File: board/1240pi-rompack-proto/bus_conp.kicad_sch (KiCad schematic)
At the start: 14 parts, among them J20 CardEdge_ROMPACK

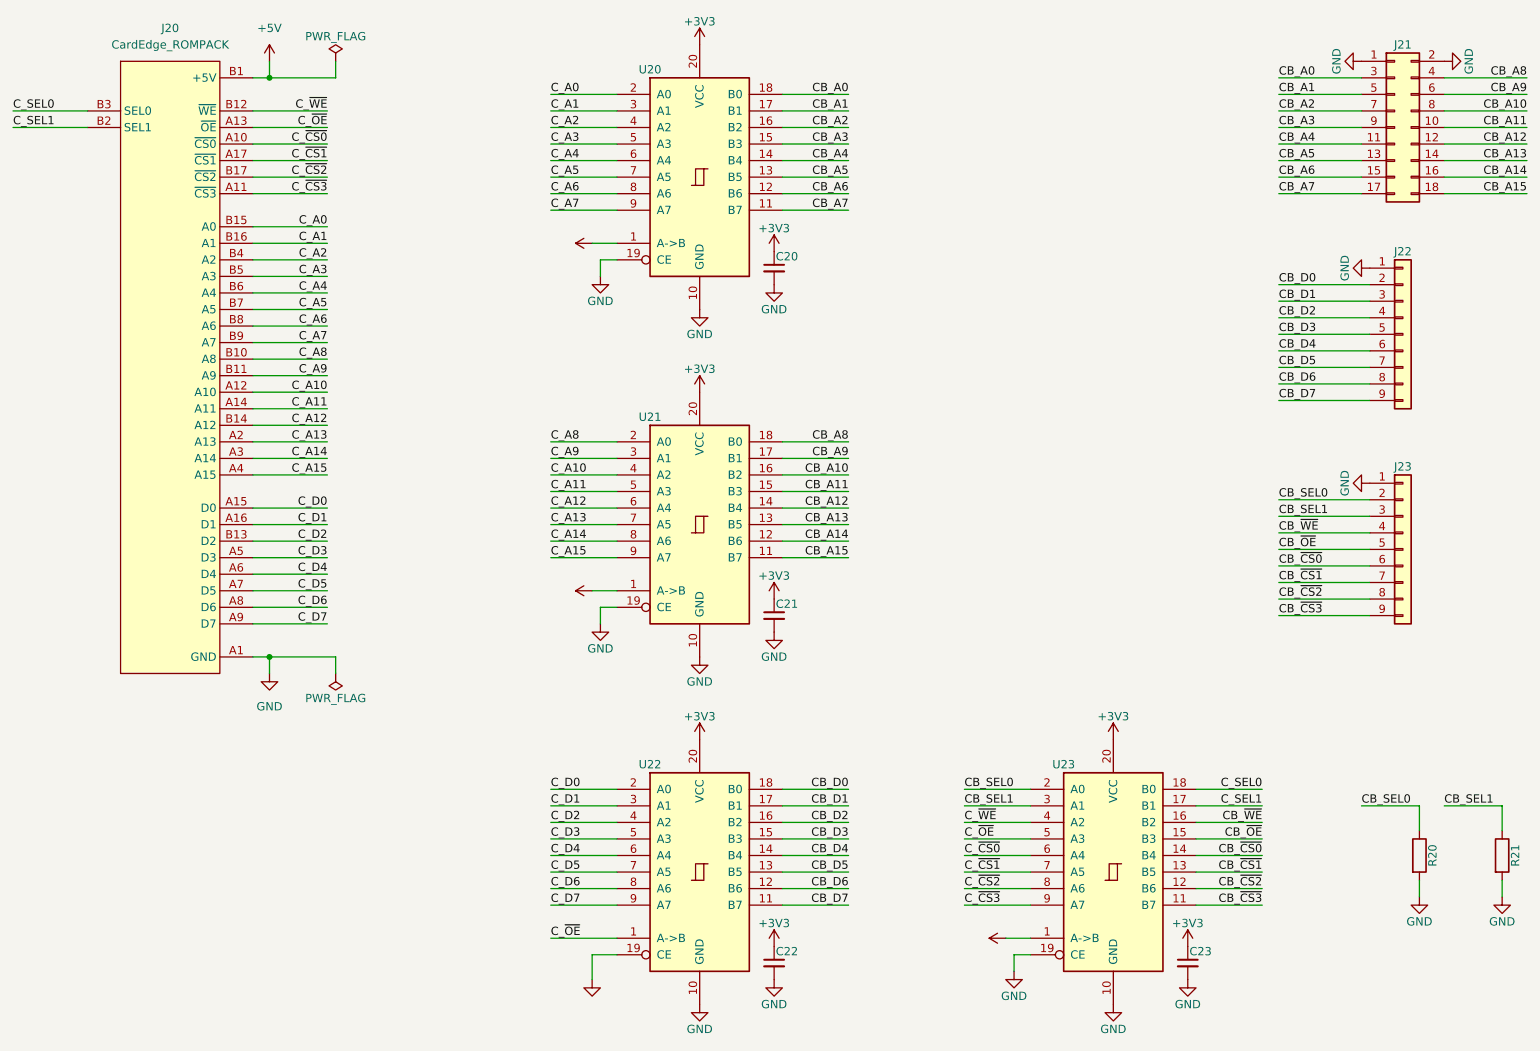
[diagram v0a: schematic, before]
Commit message: Fix names of BUSRQ and IORQ nets.
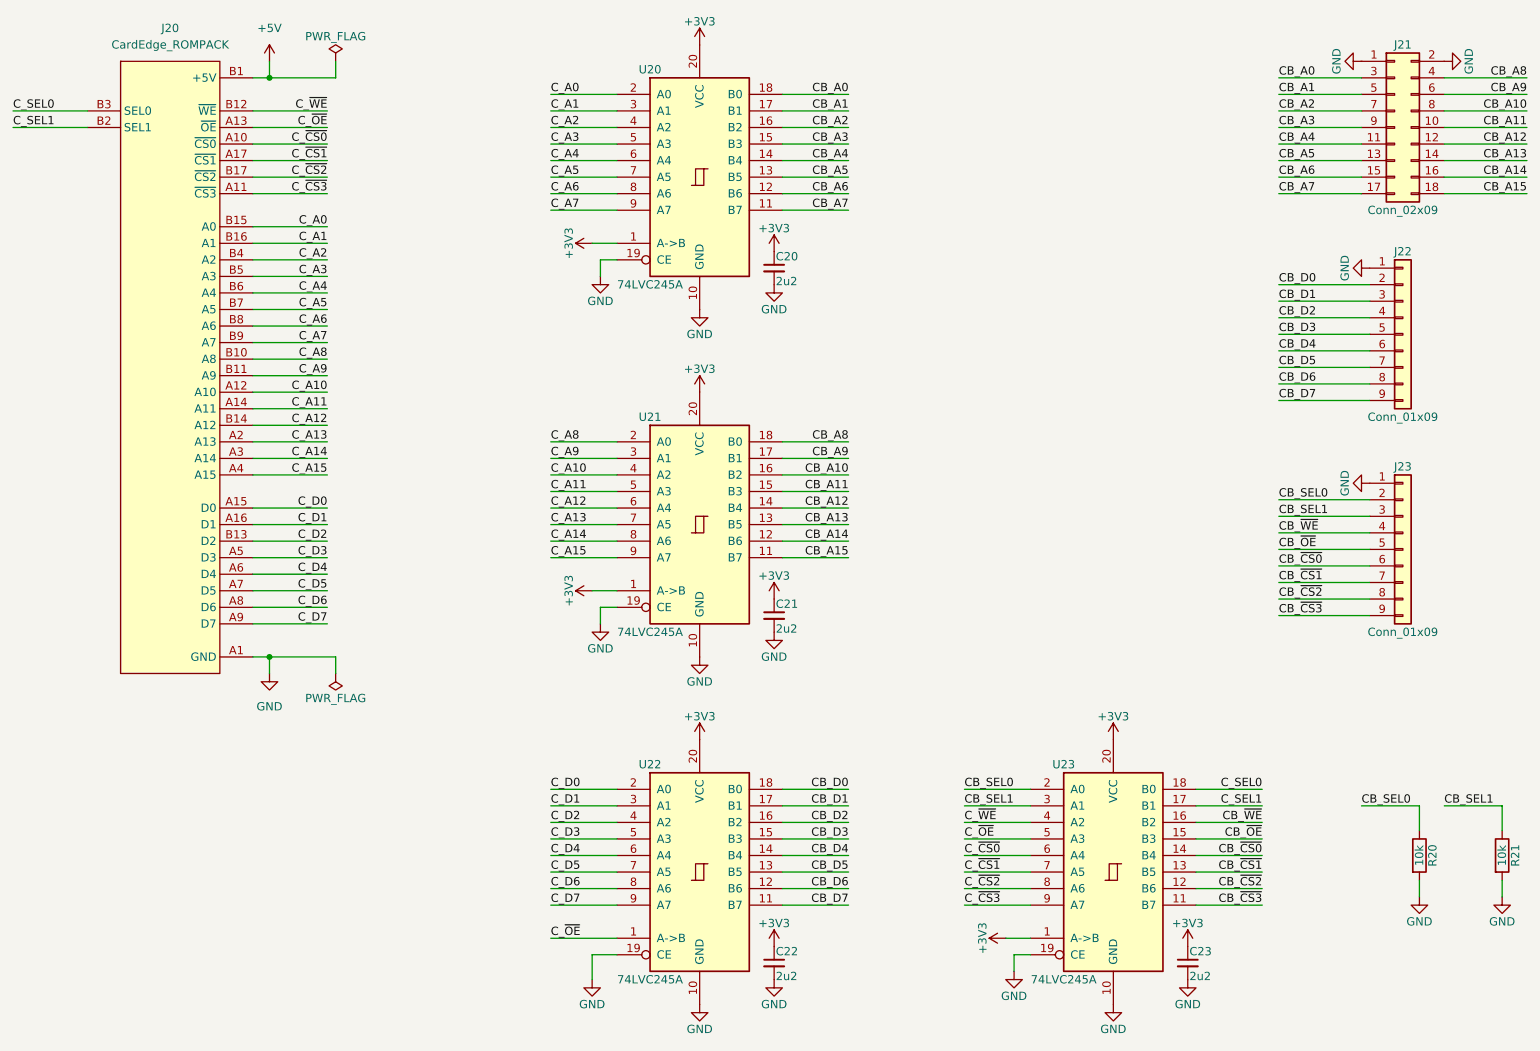
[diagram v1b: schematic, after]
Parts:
- C20, C21, C22, C23: value (none) -> 2u2; footprint (none) -> Capacitor_SMD:C_0603_1608Metric
- J21: value (none) -> Conn_02x09; footprint (none) -> Connector_PinHeader_2.54mm:PinHeader_2x09_P2.54mm_Vertical
- J22, J23: value (none) -> Conn_01x09; footprint (none) -> Connector_PinHeader_2.54mm:PinHeader_1x09_P2.54mm_Vertical
- R20, R21: value (none) -> 10k; footprint (none) -> Resistor_SMD:R_0603_1608Metric
- U20, U21, U22, U23: value (none) -> 74LVC245A; footprint (none) -> Package_SO:TSSOP-20_4.4x6.5mm_P0.65mm
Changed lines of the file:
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@@
     (in_bom yes) (on_board yes)
     (property "Reference" "R20" (id 0) (at 239.522 147.32 90))
-    (property "Value" "" (id 1) (at 237.49 147.32 90))
-    (property "Footprint" "" (id 2) (at 235.712 147.32 90)
+    (property "Value" "10k" (id 1) (at 237.49 147.32 90))
+    (property "Footprint" "Resistor_SMD:R_0603_1608Metric" (id 2) (at 235.712 147.32 90)
       (effects (font (size 1.27 1.27)) hide)
     )
@@
       (effects (font (size 1.27 1.27)) hide)
     )
-    (property "Value" "" (id 1) (at 110.49 170.18 0))
+    (property "Value" "GND" (id 1) (at 110.49 170.18 0))
     (property "Footprint" "" (id 2) (at 110.49 166.37 0)
       (effects (font (size 1.27 1.27)) hide)
@@
       (effects (font (size 1.27 1.27)) (justify left))
     )
-    (property "Value" "" (id 1) (at 138.684 112.522 0)
+    (property "Value" "2u2" (id 1) (at 138.684 112.522 0)
       (effects (font (size 1.27 1.27)) (justify left))
     )
-    (property "Footprint" "" (id 2) (at 138.43 110.49 0)
+    (property "Footprint" "Capacitor_SMD:C_0603_1608Metric" (id 2) (at 138.43 110.49 0)
       (effects (font (size 1.27 1.27)) hide)
     )
@@
       (effects (font (size 1.27 1.27)) (justify left))
     )
-    (property "Value" "" (id 1) (at 202.184 165.862 0)
+    (property "Value" "2u2" (id 1) (at 202.184 165.862 0)
       (effects (font (size 1.27 1.27)) (justify left))
     )
-    (property "Footprint" "" (id 2) (at 201.93 163.83 0)
+    (property "Footprint" "Capacitor_SMD:C_0603_1608Metric" (id 2) (at 201.93 163.83 0)
       (effects (font (size 1.27 1.27)) hide)
     )
@@
       (effects (font (size 1.27 1.27)) (justify left))
     )
-    (property "Value" "" (id 1) (at 138.684 165.862 0)
+    (property "Value" "2u2" (id 1) (at 138.684 165.862 0)
       (effects (font (size 1.27 1.27)) (justify left))
     )
-    (property "Footprint" "" (id 2) (at 138.43 163.83 0)
+    (property "Footprint" "Capacitor_SMD:C_0603_1608Metric" (id 2) (at 138.43 163.83 0)
       (effects (font (size 1.27 1.27)) hide)
     )
@@
     (in_bom yes) (on_board yes)
     (property "Reference" "R21" (id 0) (at 252.222 147.32 90))
-    (property "Value" "" (id 1) (at 250.19 147.32 90))
-    (property "Footprint" "" (id 2) (at 248.412 147.32 90)
+    (property "Value" "10k" (id 1) (at 250.19 147.32 90))
+    (property "Footprint" "Resistor_SMD:R_0603_1608Metric" (id 2) (at 248.412 147.32 90)
       (effects (font (size 1.27 1.27)) hide)
     )
@@
     (in_bom yes) (on_board yes)
     (property "Reference" "U22" (id 0) (at 119.38 133.35 0))
-    (property "Value" "" (id 1) (at 119.38 166.37 0))
-    (property "Footprint" "" (id 2) (at 127 149.86 0)
+    (property "Value" "74LVC245A" (id 1) (at 119.38 166.37 0))
+    (property "Footprint" "Package_SO:TSSOP-20_4.4x6.5mm_P0.65mm" (id 2) (at 127 149.86 0)
       (effects (font (size 1.27 1.27)) hide)
     )
@@
       (effects (font (size 1.27 1.27)) hide)
     )
-    (property "Value" "" (id 1) (at 106.934 106.68 0))
+    (property "Value" "+3V3" (id 1) (at 106.934 106.68 0))
     (property "Footprint" "" (id 2) (at 110.49 106.68 0)
       (effects (font (size 1.27 1.27)) hide)
@@
     (in_bom yes) (on_board yes)
     (property "Reference" "U20" (id 0) (at 119.38 26.67 0))
-    (property "Value" "" (id 1) (at 119.38 59.69 0))
-    (property "Footprint" "" (id 2) (at 127 43.18 0)
+    (property "Value" "74LVC245A" (id 1) (at 119.38 59.69 0))
+    (property "Footprint" "Package_SO:TSSOP-20_4.4x6.5mm_P0.65mm" (id 2) (at 127 43.18 0)
       (effects (font (size 1.27 1.27)) hide)
     )
@@
       (effects (font (size 1.27 1.27)) hide)
     )
-    (property "Value" "" (id 1) (at 106.934 53.34 0))
+    (property "Value" "+3V3" (id 1) (at 106.934 53.34 0))
     (property "Footprint" "" (id 2) (at 110.49 53.34 0)
       (effects (font (size 1.27 1.27)) hide)
@@
       (effects (font (size 1.27 1.27)) hide)
     )
-    (property "Value" "" (id 1) (at 170.434 160.02 0))
+    (property "Value" "+3V3" (id 1) (at 170.434 160.02 0))
     (property "Footprint" "" (id 2) (at 173.99 160.02 0)
       (effects (font (size 1.27 1.27)) hide)
@@
     (in_bom yes) (on_board yes)
     (property "Reference" "J21" (id 0) (at 234.95 22.86 0))
-    (property "Value" "" (id 1) (at 234.95 48.26 0))
-    (property "Footprint" "" (id 2) (at 233.68 35.56 0)
+    (property "Value" "Conn_02x09" (id 1) (at 234.95 48.26 0))
+    (property "Footprint" "Connector_PinHeader_2.54mm:PinHeader_2x09_P2.54mm_Vertical" (id 2) (at 233.68 35.56 0)
       (effects (font (size 1.27 1.27)) hide)
     )
@@
     (in_bom yes) (on_board yes)
     (property "Reference" "U21" (id 0) (at 119.38 80.01 0))
-    (property "Value" "" (id 1) (at 119.38 113.03 0))
-    (property "Footprint" "" (id 2) (at 127 96.52 0)
+    (property "Value" "74LVC245A" (id 1) (at 119.38 113.03 0))
+    (property "Footprint" "Package_SO:TSSOP-20_4.4x6.5mm_P0.65mm" (id 2) (at 127 96.52 0)
       (effects (font (size 1.27 1.27)) hide)
     )
@@
     (in_bom yes) (on_board yes)
     (property "Reference" "J23" (id 0) (at 234.95 87.63 0))
-    (property "Value" "" (id 1) (at 234.95 113.03 0))
-    (property "Footprint" "" (id 2) (at 234.95 100.33 0)
+    (property "Value" "Conn_01x09" (id 1) (at 234.95 113.03 0))
+    (property "Footprint" "Connector_PinHeader_2.54mm:PinHeader_1x09_P2.54mm_Vertical" (id 2) (at 234.95 100.33 0)
       (effects (font (size 1.27 1.27)) hide)
     )
@@
     (in_bom yes) (on_board yes)
     (property "Reference" "U23" (id 0) (at 182.88 133.35 0))
-    (property "Value" "" (id 1) (at 182.88 166.37 0))
-    (property "Footprint" "" (id 2) (at 190.5 149.86 0)
+    (property "Value" "74LVC245A" (id 1) (at 182.88 166.37 0))
+    (property "Footprint" "Package_SO:TSSOP-20_4.4x6.5mm_P0.65mm" (id 2) (at 190.5 149.86 0)
       (effects (font (size 1.27 1.27)) hide)
     )
@@
     (in_bom yes) (on_board yes)
     (property "Reference" "J22" (id 0) (at 234.95 54.61 0))
-    (property "Value" "" (id 1) (at 234.95 80.01 0))
-    (property "Footprint" "" (id 2) (at 234.95 67.31 0)
+    (property "Value" "Conn_01x09" (id 1) (at 234.95 80.01 0))
+    (property "Footprint" "Connector_PinHeader_2.54mm:PinHeader_1x09_P2.54mm_Vertical" (id 2) (at 234.95 67.31 0)
       (effects (font (size 1.27 1.27)) hide)
     )
@@
       (effects (font (size 1.27 1.27)) (justify left))
     )
-    (property "Value" "" (id 1) (at 138.684 59.182 0)
+    (property "Value" "2u2" (id 1) (at 138.684 59.182 0)
       (effects (font (size 1.27 1.27)) (justify left))
     )
-    (property "Footprint" "" (id 2) (at 138.43 57.15 0)
-      (effects (font (size 1.27 1.27)) hide)
-    )
+    (property "Footprint" "Capacitor_SMD:C_0603_1608Metric" (id 2) (at 138.43 57.15 0)
+      (effects (font (size 1.27 1.27)) hide)
+    )
